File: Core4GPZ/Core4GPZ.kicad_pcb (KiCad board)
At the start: 2 copper layers, 99.1 x 114.3 mm, 17 parts, among them J1 Delphi_Sicma_24, J2 Delphi_Sicma_24, Q1 IRG4PF50W, Q5 IRG4PF50W, U1 core4, U2 MPX4250

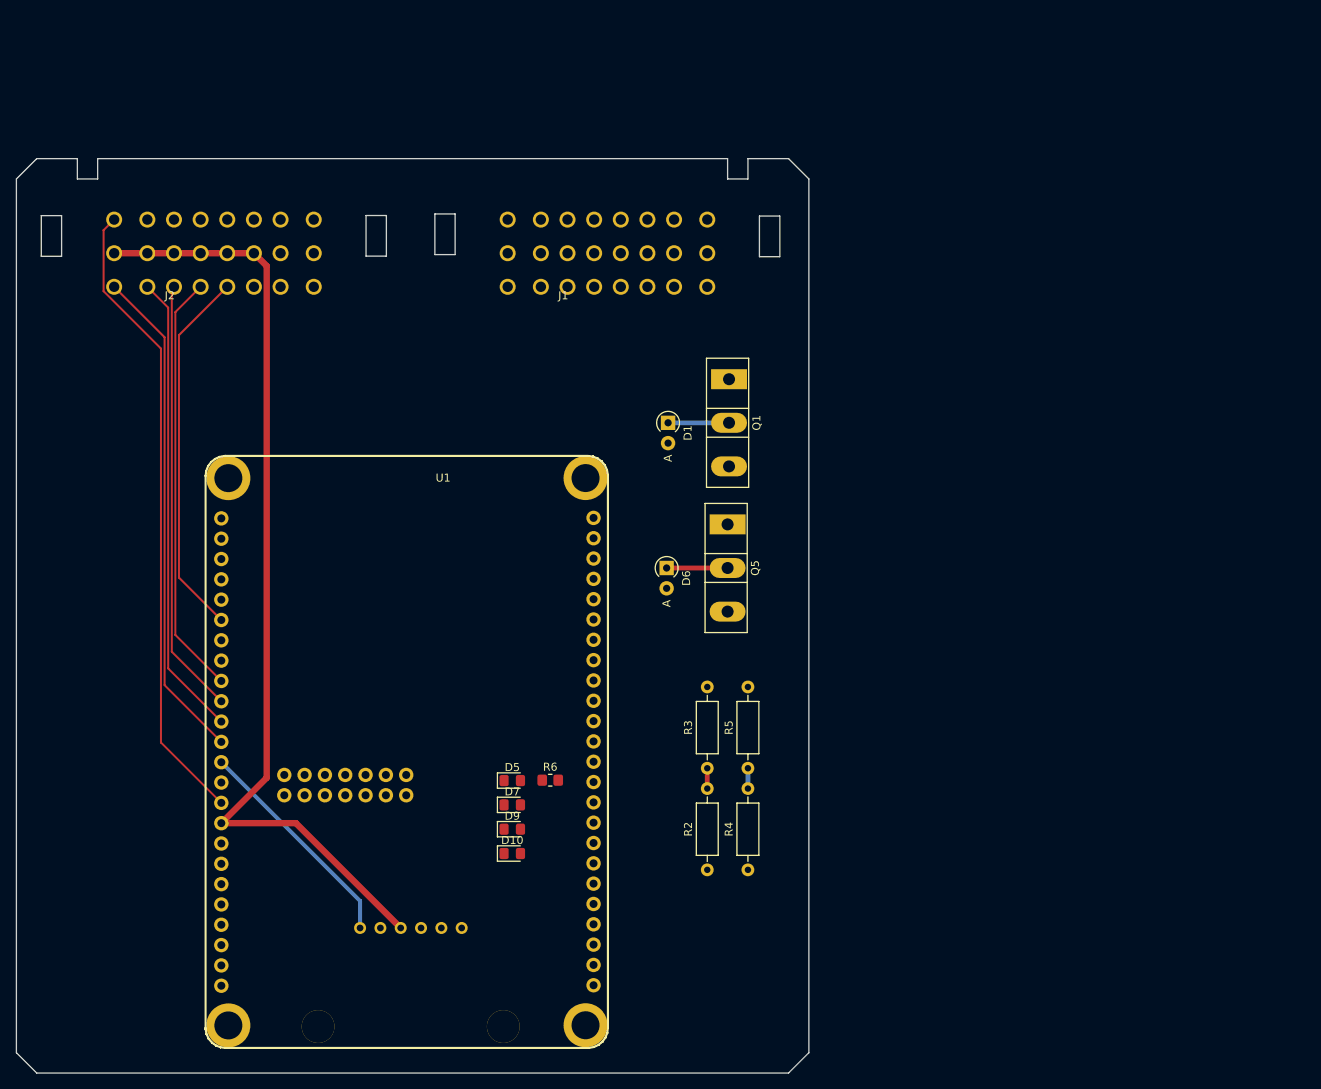
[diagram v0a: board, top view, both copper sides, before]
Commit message: Changed Connectors for Molex CMC 48pins Black.
Changed ECU Connector for Molex CMC 48pins Black, for compacity and cost reduction. Designed custom Footprint for this purpose
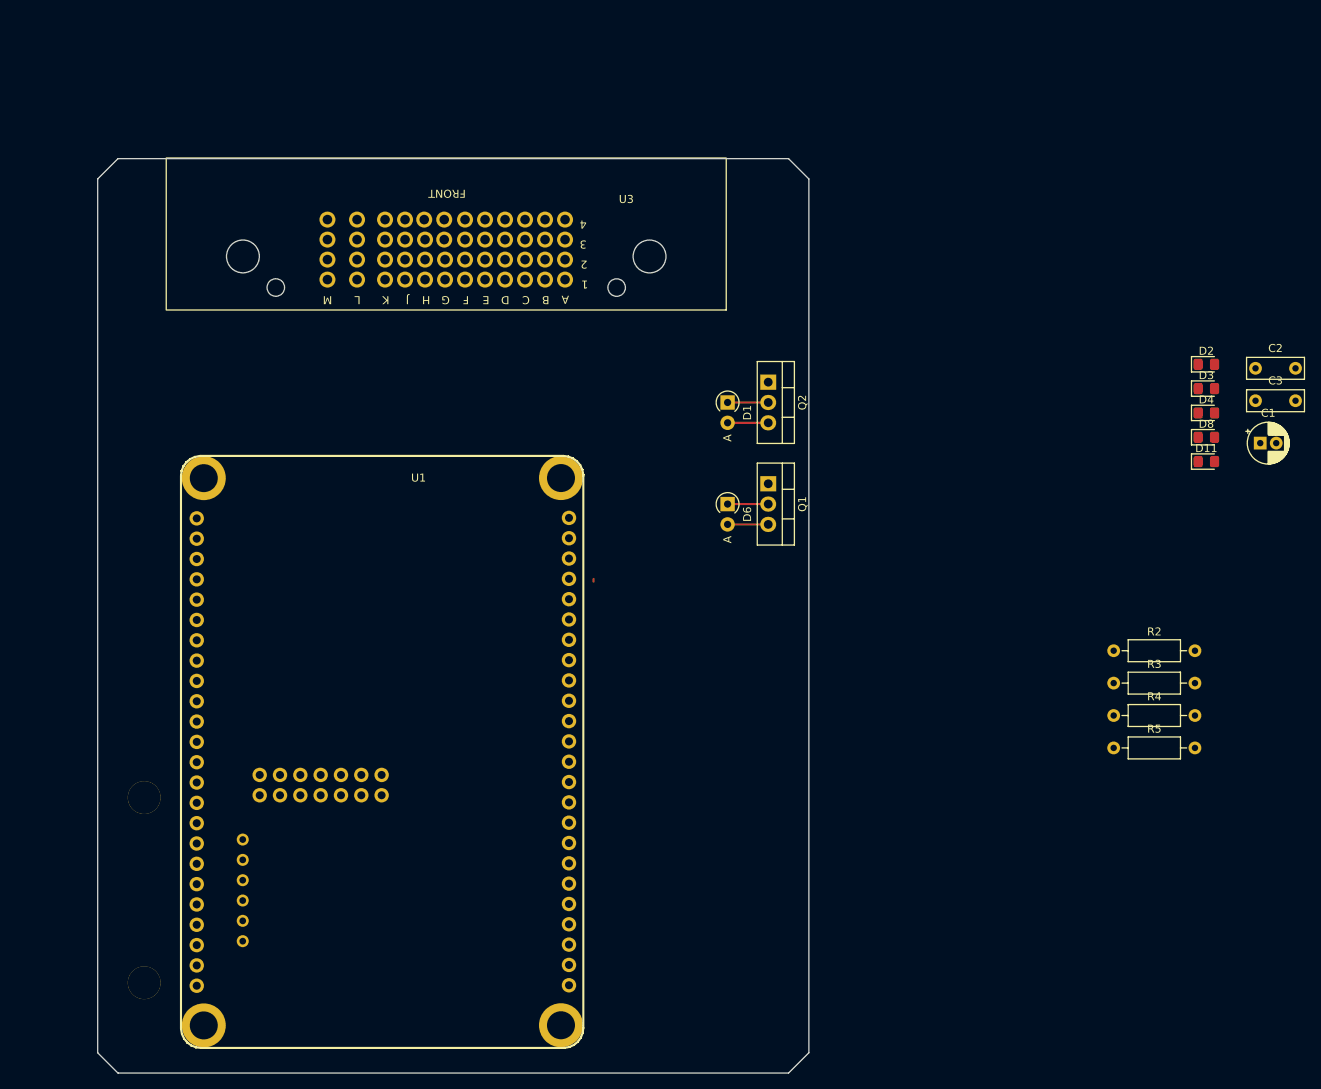
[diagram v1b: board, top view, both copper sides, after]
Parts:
- removed D10, D5, D7, D9: D, Diode_SMD:D_0805_2012Metric_Pad1.15x1.40mm_HandSolder
- removed J1: Delphi_Sicma_24, Speeduino_Conn_Automotive:Delphi_Sicma_24_Black
- removed J2: Delphi_Sicma_24, Speeduino_Conn_Automotive:Delphi_Sicma_24_Grey
- removed Q5: IRG4PF50W, Package_TO_SOT_THT:TO-247-3_Vertical
- removed R6: 1k, Resistor_SMD:R_0805_2012Metric_Pad1.20x1.40mm_HandSolder
- added C1: 10uF, Capacitor_THT:CP_Radial_D5.0mm_P2.00mm, F.Cu at (198.7, 76.2)
- added C2: 100nF, Capacitor_THT:C_Rect_L7.0mm_W2.5mm_P5.00mm, F.Cu at (198.1, 66.8)
- added C3: 1nF, Capacitor_THT:C_Rect_L7.0mm_W2.5mm_P5.00mm, F.Cu at (198.1, 70.9)
- added D11: D, Diode_SMD:D_0805_2012Metric_Pad1.15x1.40mm_HandSolder, F.Cu at (191.9, 78.5)
- added D2: D, Diode_SMD:D_0805_2012Metric_Pad1.15x1.40mm_HandSolder, F.Cu at (191.9, 66.3)
- added D3: D, Diode_SMD:D_0805_2012Metric_Pad1.15x1.40mm_HandSolder, F.Cu at (191.9, 69.4)
- added D4: D, Diode_SMD:D_0805_2012Metric_Pad1.15x1.40mm_HandSolder, F.Cu at (191.9, 72.4)
- added D8: D, Diode_SMD:D_0805_2012Metric_Pad1.15x1.40mm_HandSolder, F.Cu at (191.9, 75.5)
- added Q2: IRF740, Package_TO_SOT_THT:TO-220-3_Vertical, F.Cu at (137.2, 68.6)
- added U3: ~, Molex_CMC_Conn:Molex_CMC_48pin_Male_Black, F.Cu at (96.9, 40.6)
- Q1: value IRG4PF50W -> IRF740; footprint Package_TO_SOT_THT:TO-247-3_Vertical -> Package_TO_SOT_THT:TO-220-3_Vertical
- moved R2 57.7 mm to (180.3, 102.2), turned to 0 degrees
- moved R3 51.9 mm to (180.3, 106.2), turned to 0 degrees
- moved R4 49.6 mm to (180.3, 110.2), turned to 0 degrees
- moved R5 45.8 mm to (180.3, 114.3), turned to 0 degrees
- moved U2 18.4 mm to (71.5, 125.8), turned to -90 degrees
- moved Q1 14.0 mm to (137.2, 81.3)
- moved D6 11.0 mm to (132.1, 83.8)
- moved D1 7.86 mm to (132.1, 71.1)
- moved U1 3.07 mm to (112.3, 144.0)
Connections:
- net +5V renamed CLT_+5V
- D1 pad 2: GND -> BIKE_GROUND
- D6 pad 2: GND -> BIKE_GROUND
- Q1 pad 2: IGN_COIL2_DRIVE -> IGN_COIL1_DRIVE
- Q1 pad 3: GND -> BIKE_GROUND
- R2 pad 2: Net-(Q5-G) -> Net-(Q1-G)
- R3 pad 1: Net-(Q5-G) -> Net-(Q1-G)
- R3 pad 2: GND -> BIKE_GROUND
- R4 pad 2: Net-(Q1-G) -> Net-(Q2-G)
- R5 pad 1: Net-(Q1-G) -> Net-(Q2-G)
- R5 pad 2: GND -> BIKE_GROUND
- U1 pad 17: unconnected-(U1A-D36-Pad17) -> /NEUTRAL_LIGHT
- U1 pad 20: /NEUTRAL_LIGHT -> unconnected-(U1A-D33-Pad20)
- U1 pad 23: unconnected-(U1A-IGN3-Pad23) -> IGN_TRIG_3
- U1 pad 24: unconnected-(U1A-IGN4-Pad24) -> IGN_TRIG_4
- U1 pad 25: +12V -> BIKE_+12V_SWITCHED_IN
- U1 pad 26: unconnected-(U1B-EARTH-Pad26) -> BIKE_GROUND
- U1 pad 27: unconnected-(U1B-EARTH-Pad27) -> BIKE_GROUND
- U1 pad 28: unconnected-(U1B-EARTH-Pad28) -> BIKE_GROUND
- U1 pad 29: unconnected-(U1B-EARTH-Pad29) -> BIKE_GROUND
- U1 pad 30: unconnected-(U1B-EARTH-Pad30) -> BIKE_GROUND
- U1 pad 31: unconnected-(U1B-EARTH-Pad31) -> BIKE_GROUND
- U1 pad 32: unconnected-(U1B-EARTH-Pad32) -> BIKE_GROUND
- U1 pad 35: unconnected-(U1B-RPM2-Pad35) -> /CAM_SNSR
- U1 pad 5: unconnected-(U1A-INJ3-Pad5) -> /INJ3_TRIG
- U1 pad 7: unconnected-(U1A-INJ4-Pad7) -> /INJ4_TRIG
- U2 pad 2: GND -> BIKE_GROUND
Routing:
- net CLT_+5V: track 119.6 -> 0.00 mm
- net /CRANK_SNSR: track 79.6 -> 0.00 mm
- net /TPS_SNSR: track 62.4 -> 0.00 mm
- net /CLT_SNSR: track 58.2 -> 0.00 mm
- net /IAT_SNSR: track 55.4 -> 0.00 mm
- net /O2WB_SNSR: track 53.0 -> 0.00 mm
- net /FLEX_SNSR: track 47.1 -> 0.00 mm
- net Net-(U1B-MAP_IN): track 27.9 -> 0.00 mm
- net BIKE_GROUND: track 0.00 -> 10.2 mm
- net IGN_COIL1_DRIVE: track 7.62 -> 5.08 mm
- net IGN_COIL2_DRIVE: track 7.62 -> 5.08 mm
- net Net-(Q5-G): track 2.54 -> 0.00 mm
- net Net-(Q1-G): track 2.54 -> 0.00 mm
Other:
- board size 99.1 x 114.3 mm -> 88.9 x 114.3 mm

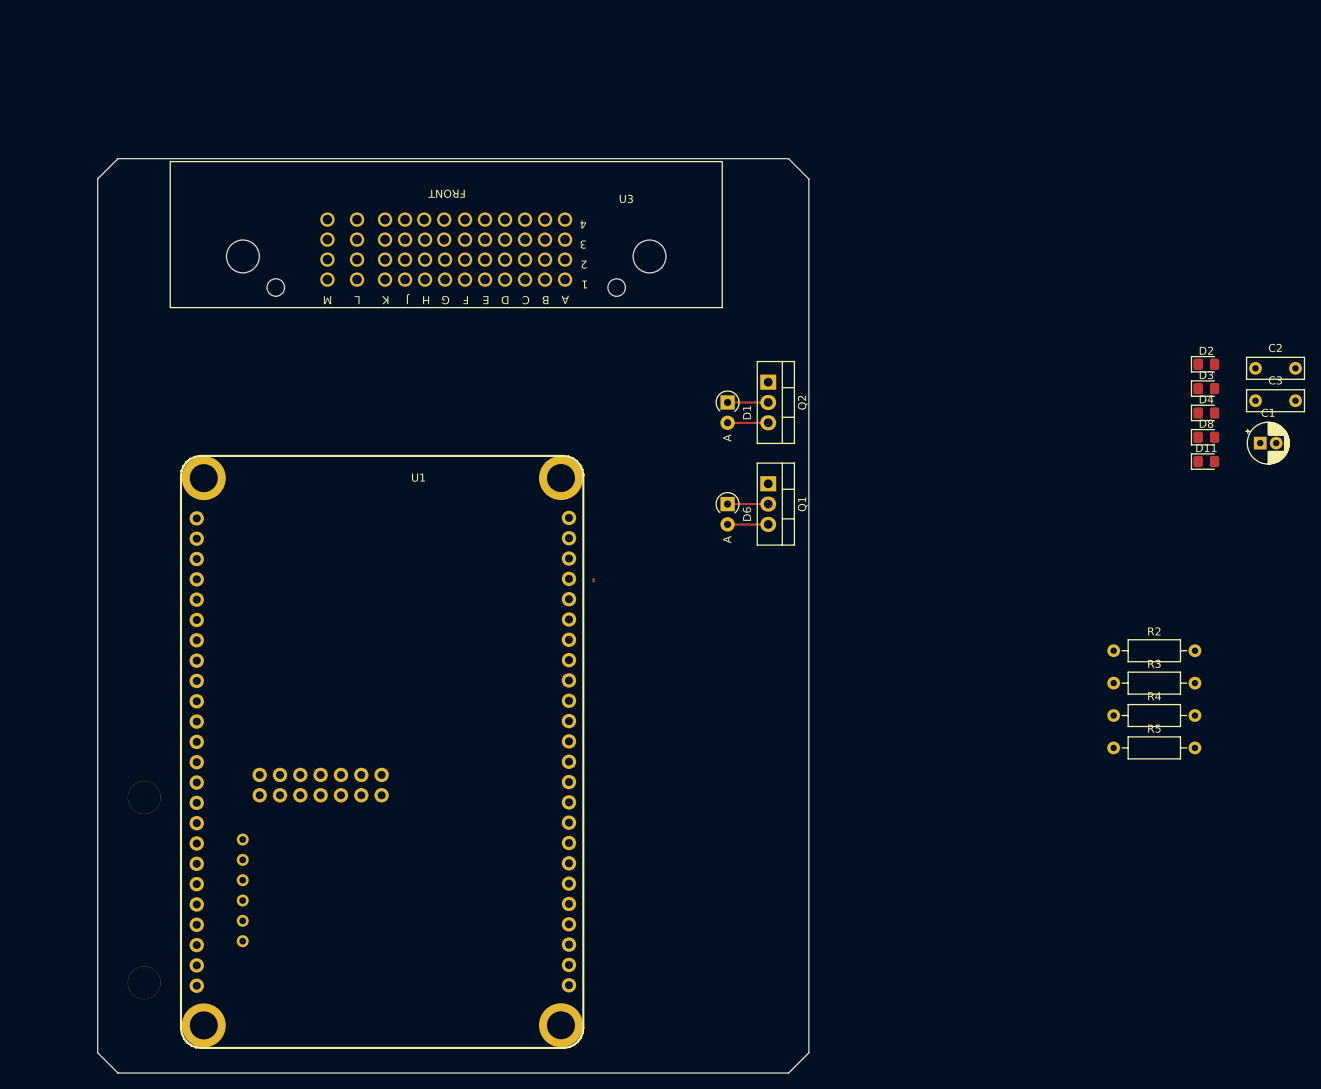
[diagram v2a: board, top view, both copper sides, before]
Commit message: Added VR Conditionner for Cam/Crank SNSR
Added some jumper for prototyping and testing purposes
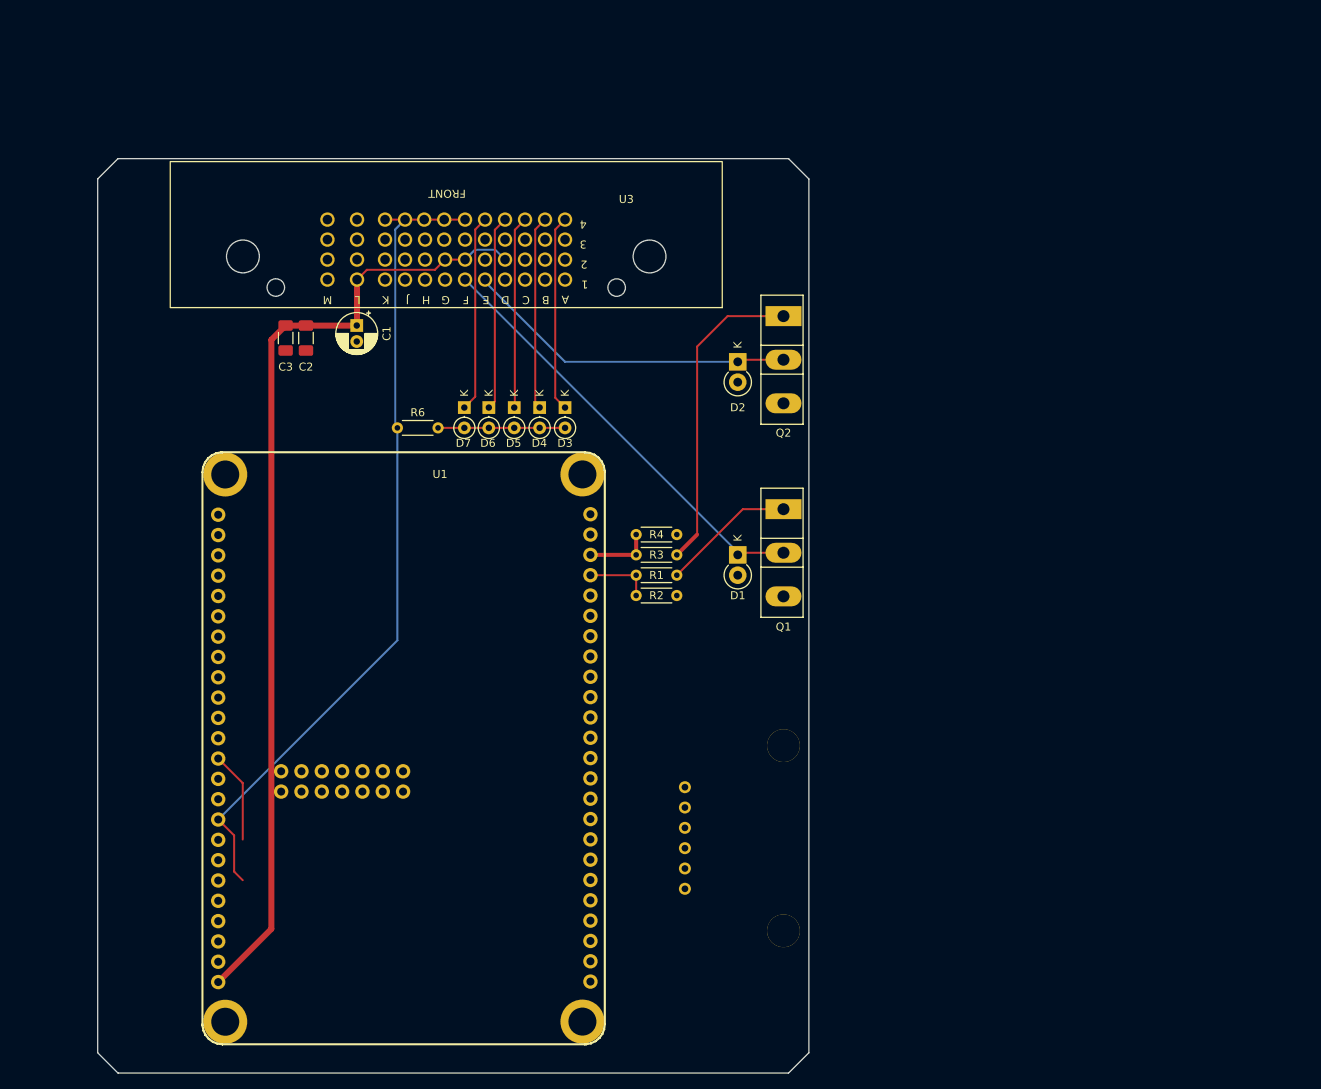
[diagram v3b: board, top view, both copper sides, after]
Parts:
- removed D11, D8: D, Diode_SMD:D_0805_2012Metric_Pad1.15x1.40mm_HandSolder
- removed R5: 10k, Resistor_THT:R_Axial_DIN0207_L6.3mm_D2.5mm_P10.16mm_Horizontal
- added D5: D, Diode_THT:D_DO-35_SOD27_P2.54mm_Vertical_KathodeUp, F.Cu at (105.4, 71.8)
- added D7: D, Diode_THT:D_DO-35_SOD27_P2.54mm_Vertical_KathodeUp, F.Cu at (99.2, 71.8)
- added R1: 1k, Resistor_THT:R_Axial_DIN0204_L3.6mm_D1.6mm_P5.08mm_Horizontal, F.Cu at (125.7, 92.7)
- added R6: 100k, Resistor_THT:R_Axial_DIN0204_L3.6mm_D1.6mm_P5.08mm_Horizontal, F.Cu at (90.8, 74.3)
- C2, C3: footprint Capacitor_THT:C_Rect_L7.0mm_W2.5mm_P5.00mm -> Capacitor_SMD:C_1206_3216Metric_Pad1.33x1.80mm_HandSolder
- D1: footprint Diode_THT:D_A-405_P2.54mm_Vertical_AnodeUp -> Diode_THT:D_DO-41_SOD81_P2.54mm_Vertical_KathodeUp
- D2: value D -> 1N4007; footprint Diode_SMD:D_0805_2012Metric_Pad1.15x1.40mm_HandSolder -> Diode_THT:D_DO-41_SOD81_P2.54mm_Vertical_KathodeUp
- D3, D4: footprint Diode_SMD:D_0805_2012Metric_Pad1.15x1.40mm_HandSolder -> Diode_THT:D_DO-35_SOD27_P2.54mm_Vertical_KathodeUp
- D6: value 1N4007 -> D; footprint Diode_THT:D_A-405_P2.54mm_Vertical_AnodeUp -> Diode_THT:D_DO-35_SOD27_P2.54mm_Vertical_KathodeUp
- Q1, Q2: value IRF740 -> IRG4PF50W; footprint Package_TO_SOT_THT:TO-220-3_Vertical -> Package_TO_SOT_THT:TO-247-3_Vertical
- R2, R4: value 1k -> 10k; footprint Resistor_THT:R_Axial_DIN0207_L6.3mm_D2.5mm_P10.16mm_Horizontal -> Resistor_THT:R_Axial_DIN0204_L3.6mm_D1.6mm_P5.08mm_Horizontal
- R3: value 10k -> 1k; footprint Resistor_THT:R_Axial_DIN0207_L6.3mm_D2.5mm_P10.16mm_Horizontal -> Resistor_THT:R_Axial_DIN0204_L3.6mm_D1.6mm_P5.08mm_Horizontal
- moved C3 121.5 mm to (76.8, 63.1), turned to -90 degrees
- moved C2 118.8 mm to (79.4, 63.1), turned to -90 degrees
- moved C1 113.9 mm to (85.7, 61.5), turned to -90 degrees
- moved D4 83.3 mm to (108.6, 71.8), turned to -90 degrees
- moved D3 80.2 mm to (111.8, 71.8), turned to -90 degrees
- moved R4 63.8 mm to (120.7, 87.6)
- moved R2 60.1 mm to (120.7, 95.2)
- moved D2 58.6 mm to (133.3, 66.0), turned to -90 degrees
- moved R3 56.9 mm to (125.7, 90.2), turned to 180 degrees
- moved U2 55.6 mm to (126.7, 131.9), turned to 90 degrees
- moved D6 32.2 mm to (102.2, 71.8)
- moved D1 19.1 mm to (133.3, 90.2)
- moved Q2 8.47 mm to (139.1, 60.3)
- moved Q1 3.70 mm to (139.1, 84.5)
- moved U1 2.72 mm to (114.9, 143.5)
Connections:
- D1 pad 1: IGN_COIL2_DRIVE -> IGN_COIL1_DRIVE
- D2 pad 1: SideStand_SWITCH -> IGN_COIL2_DRIVE
- D2 pad 2: SAFE_SIGNAL -> BIKE_GROUND
- D3 pad 1: Neutral_SWITCH -> SideStand_SWITCH
- D4 pad 1: Clutch_SWITCH -> Neutral_SWITCH
- D6 pad 1: IGN_COIL1_DRIVE -> SPR1_SWITCH
- D6 pad 2: BIKE_GROUND -> SAFE_SIGNAL
- R2 pad 2: Net-(Q1-G) -> BIKE_GROUND
- R3 pad 1: Net-(Q1-G) -> Net-(Q2-G)
- R3 pad 2: BIKE_GROUND -> IGN_TRIG_2
- R4 pad 2: Net-(Q2-G) -> BIKE_GROUND
- U1 pad 21: IGN_TRIG_2 -> IGN_TRIG_1
- U1 pad 22: IGN_TRIG_1 -> IGN_TRIG_2
- U1 pad 40: /O2WB_SNSR -> /O2_SNSR
- U1 pad 61: unconnected-(U1C-EARTH-Pad61) -> BIKE_+12V_SWITCHED_IN
- U1 pad 62: unconnected-(U1C-+5V-Pad62) -> BIKE_+12V_SWITCHED_IN
- U3 pad 22: BIKE_GROUND -> /CAM_SNSR
- U3 pad 23: /CAM_SNSR -> unconnected-(U3B-3C-Pad23)
- U3 pad 24: BIKE_GROUND -> unconnected-(U3B-3D-Pad24)
- U3 pad 27: /O2WB_SNSR -> /02_SNSR
- U3 pad 31: unconnected-(U3B-4A-Pad31) -> SideStand_SWITCH
- U3 pad 32: unconnected-(U3B-4B-Pad32) -> Neutral_SWITCH
- U3 pad 33: unconnected-(U3B-4C-Pad33) -> Clutch_SWITCH
- U3 pad 34: unconnected-(U3B-4D-Pad34) -> SPR1_SWITCH
- U3 pad 35: unconnected-(U3B-4E-Pad35) -> SPR2_SWITCH
- U3 pad 36: unconnected-(U3B-4F-Pad36) -> CLT_+5V
- U3 pad 37: unconnected-(U3B-4G-Pad37) -> CLT_+5V
- U3 pad 38: unconnected-(U3B-4H-Pad38) -> CLT_+5V
- U3 pad 39: unconnected-(U3B-4J-Pad39) -> CLT_+5V
- U3 pad 40: unconnected-(U3B-4K-Pad40) -> CLT_+5V
- U3 pad 41: BIKE_GROUND -> BIKE_+12V_SWITCHED_IN
- U3 pad 48: BIKE_+12V_SWITCHED_IN -> BIKE_GROUND
- U3 pad 5: IGN_COIL1_DRIVE -> IGN_COIL2_DRIVE
- U3 pad 6: IGN_COIL2_DRIVE -> IGN_COIL1_DRIVE
- U3 pad 7: IGN_COIL3_DRIVE -> unconnected-(U3A-1G-Pad7)
- U3 pad 8: IGN_COIL4_DRIVE -> unconnected-(U3A-1H-Pad8)
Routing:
- net BIKE_+12V_SWITCHED_IN: track 0.00 -> 120.8 mm
- net CLT_+5V: track 0.00 -> 103.7 mm
- net IGN_COIL1_DRIVE: track 5.08 -> 54.4 mm
- net Net-(Q2-G): track 0.00 -> 39.5 mm
- net IGN_COIL2_DRIVE: track 5.08 -> 41.8 mm
- net SPR2_SWITCH: track 0.00 -> 24.6 mm
- net SideStand_SWITCH: track 0.00 -> 24.5 mm
- net SPR1_SWITCH: track 0.00 -> 24.3 mm
- net Neutral_SWITCH: track 0.00 -> 24.2 mm
- net Clutch_SWITCH: track 0.00 -> 24.1 mm
- net Net-(Q1-G): track 0.00 -> 16.8 mm
- net SAFE_SIGNAL: track 0.00 -> 15.9 mm
- net Net-(U1B-MAP_IN): track 0.00 -> 11.4 mm
- net BIKE_GROUND: track 10.2 -> 0.00 mm
- net IGN_TRIG_1: track 0.00 -> 8.26 mm
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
